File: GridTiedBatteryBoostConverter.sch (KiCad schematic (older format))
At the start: 58 parts, among them J101 Battery Connection, J103 Solar Panels, Q101 IXFP36N20X3, Q102 BC847B-13-F, Q103 SSM3K329R, Q104 SSM3J334R, U101 OPA2837DGK, U102 UCC2800DTR

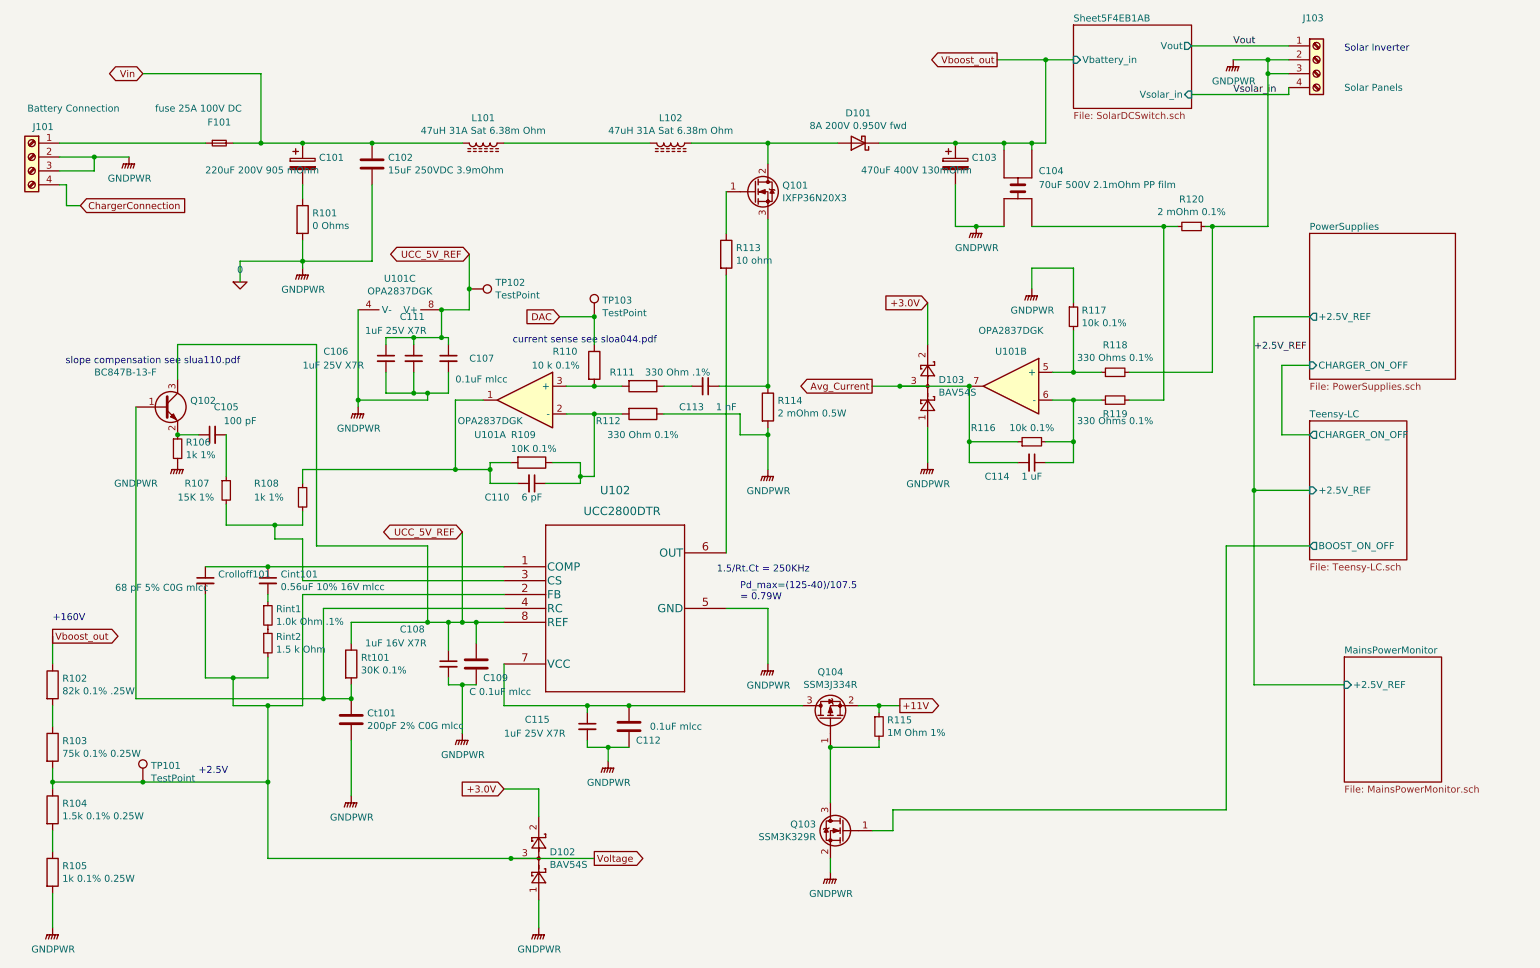
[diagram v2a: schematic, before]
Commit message: Consolidated a lot of part values that were the same part but not detected the same by Boms_away BOM editor because of subtle differences in how I specified the values. Added Digi-key part numbers to the resistors. Replaced 2mOhm .5W current sense resistors with 1W 2mOhm Thin Film resistors (lower inductance than metal element), And fixed a bug where I was earthing the return feed of the Solar inverter before passing through the current sense resistor.
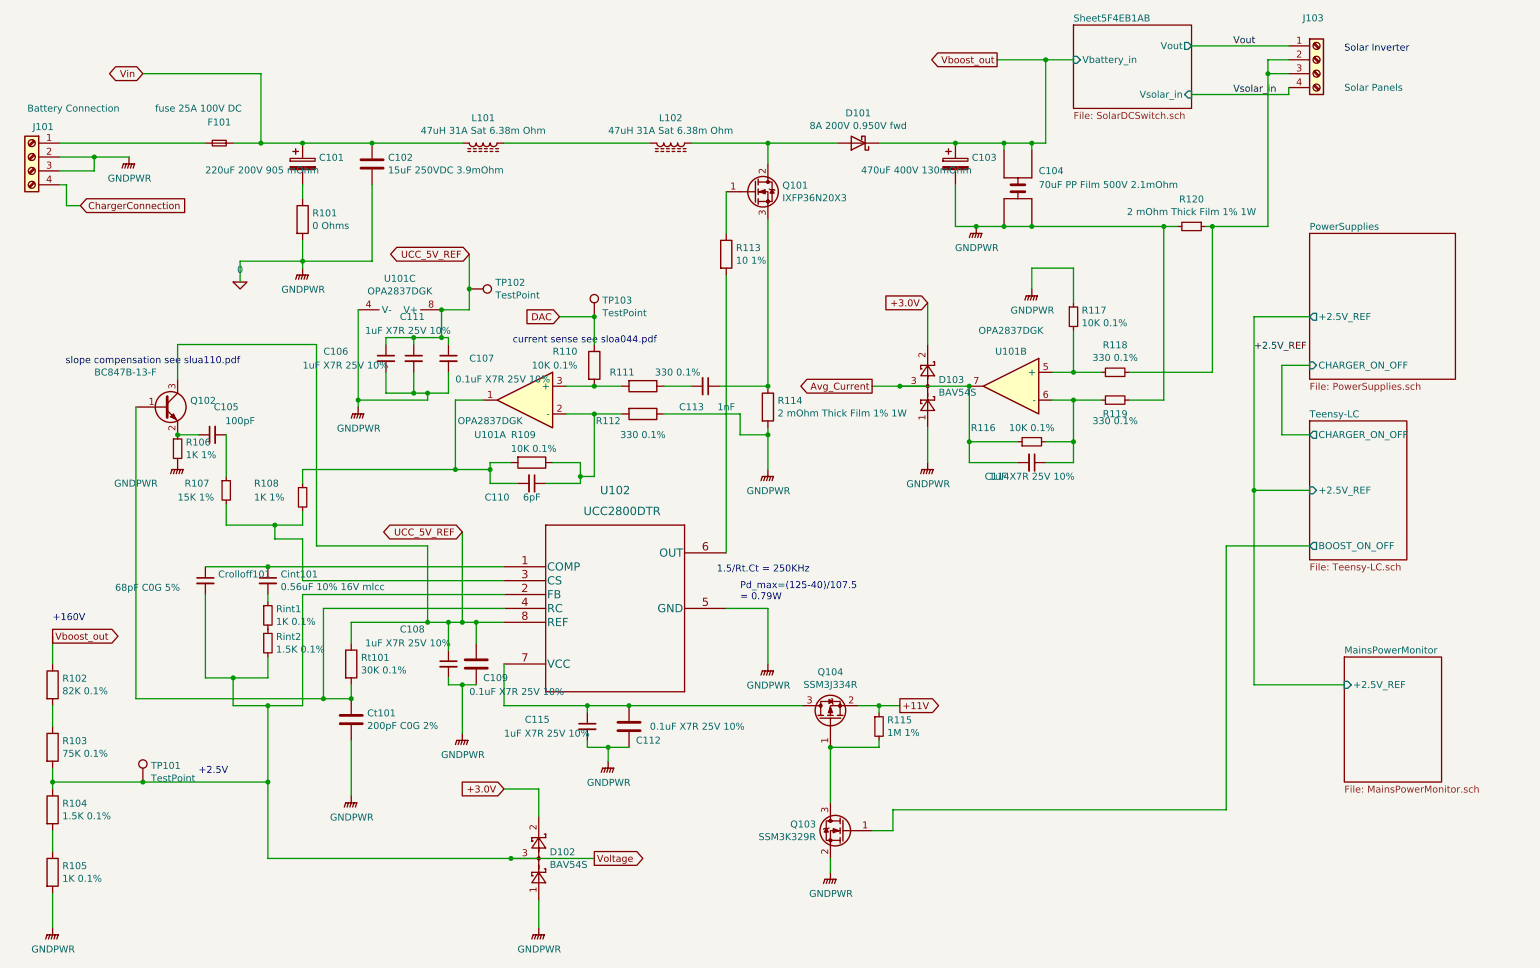
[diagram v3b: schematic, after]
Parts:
- C101, C102, C103, Cint101, D101, D102, D103, F101, J101, J103, L102, Q101, Q102, Q103, Q104, TP101, TP102, TP103, U101, U102: MFR (none) -> -; MPN (none) -> -; SPN (none) -> -; SPR (none) -> -; SPURL (none) -> -
- C104: value 70uF 500V 2.1mOhm PP film -> 70uF PP Film 500V 2.1mOhm; MFR (none) -> -; MPN (none) -> -; SPN (none) -> -; SPR (none) -> -; SPURL (none) -> -
- C105: value 100 pF -> 100pF; MFR (none) -> -; MPN (none) -> -; SPN (none) -> -; SPR (none) -> -; SPURL (none) -> -
- C106, C111, C115: value 1uF 25V X7R -> 1uF X7R 25V 10%; MFR (none) -> Wurth Elektronik; MPN (none) -> 885012207078; SPN (none) -> 732-7672-1-ND; SPR (none) -> digikey; SPURL (none) -> -
- C107, C112: value 0.1uF mlcc -> 0.1uF X7R 25V 10%; MFR (none) -> Samsung; MPN (none) -> CL21B104KACNNNC; SPN (none) -> 1276-1099-1-ND; SPR (none) -> digikey; SPURL (none) -> -
- C108: value 1uF 16V X7R -> 1uF X7R 25V 10%; MFR (none) -> Wurth Elektronik; MPN (none) -> 885012207078; SPN (none) -> 732-7672-1-ND; SPR (none) -> digikey; SPURL (none) -> -
- C109: value C 0.1uF mlcc -> 0.1uF X7R 25V 10%; MFR (none) -> Samsung; MPN (none) -> CL21B104KACNNNC; SPN (none) -> 1276-1099-1-ND; SPR (none) -> digikey; SPURL (none) -> -
- C110: value 6 pF -> 6pF; MFR (none) -> -; MPN (none) -> -; SPN (none) -> -; SPR (none) -> -; SPURL (none) -> -
- C113: value 1 nF -> 1nF; MFR (none) -> -; MPN (none) -> -; SPN (none) -> -; SPR (none) -> -; SPURL (none) -> -
- C114: value 1 uF -> 1uF X7R 25V 10%; MFR (none) -> Wurth Elektronik; MPN (none) -> 885012207078; SPN (none) -> 732-7672-1-ND; SPR (none) -> digikey; SPURL (none) -> -
- Crolloff101: value 68 pF 5% C0G mlcc -> 68pF C0G 5%; MFR (none) -> -; MPN (none) -> -; SPN (none) -> -; SPR (none) -> -; SPURL (none) -> -
- Ct101: value 200pF 2% C0G mlcc -> 200pF C0G 2%; MFR (none) -> AVX Corporation; MPN (none) -> 08051A201GAT2A; SPN (none) -> 478-10384-1-ND; SPR (none) -> digikey; SPURL (none) -> -
- L101: value 47uH 31A Sat 6.38m Ohm -> 47uH 31A Sat 6.38m Ohm; MFR (none) -> -; MPN (none) -> -; SPN (none) -> -; SPR (none) -> -; SPURL (none) -> -
- R101: MFR (none) -> Stackpole Electronics Inc; MPN (none) -> RMCF0805ZT0R00; SPN (none) -> RMCF0805ZT0R00CT-ND; SPR (none) -> digikey; SPURL (none) -> -
- R102: value 82k 0.1% .25W -> 82K 0.1%; MFR (none) -> Panasonic Electronic Components; MPN (none) -> ERA-6AEB823V; SPN (none) -> P82KDACT-ND; SPR (none) -> digikey; SPURL (none) -> -
- R103: value 75k 0.1% 0.25W -> 75K 0.1%; MFR (none) -> Panasonic Electronic Components; MPN (none) -> ERJ-PB6B7502V; SPN (none) -> P20808CT-ND; SPR (none) -> digikey; SPURL (none) -> -
- R104: value 1.5k 0.1% 0.25W -> 1.5K 0.1%; MFR (none) -> Panasonic Electronic Components; MPN (none) -> ERA-6AEB152V; SPN (none) -> P1.5KDACT-ND; SPR (none) -> digikey; SPURL (none) -> -
- R105: value 1k 0.1% 0.25W -> 1K 0.1%; MFR (none) -> Panasonic Electronic Components; MPN (none) -> ERA-6AEB102V; SPN (none) -> P1.0KDACT-ND; SPR (none) -> digikey; SPURL (none) -> -
- R106, R108: value 1k 1% -> 1K 1%; MFR (none) -> Yageo; MPN (none) -> RC0805FR-071KL; SPN (none) -> 311-1.00KCRCT-ND; SPR (none) -> digikey; SPURL (none) -> -
- R107: MFR (none) -> TE Connectivity Passive Product; MPN (none) -> CRGCQ0805F15K; SPN (none) -> A129763CT-ND; SPR (none) -> digikey; SPURL (none) -> -
- R109: MFR (none) -> Panasonic Electronic Components; MPN (none) -> ERA-6AEB103V; SPN (none) -> P10KDACT-ND; SPR (none) -> digikey; SPURL (none) -> -
- R110: value 10 k 0.1% -> 10K 0.1%; MFR (none) -> Panasonic Electronic Components; MPN (none) -> ERA-6AEB103V; SPN (none) -> P10KDACT-ND; SPR (none) -> digikey; SPURL (none) -> -
- R111: value 330 Ohm .1% -> 330 0.1%; MFR (none) -> Panasonic Electronic Components; MPN (none) -> ERA-6AEB331V; SPN (none) -> P330DACT-ND; SPR (none) -> digikey; SPURL (none) -> -
- R112: value 330 Ohm 0.1% -> 330 0.1%; MFR (none) -> Panasonic Electronic Components; MPN (none) -> ERA-6AEB331V; SPN (none) -> P330DACT-ND; SPR (none) -> digikey; SPURL (none) -> -
- R113: value 10 ohm -> 10 1%; MFR (none) -> Yageo; MPN (none) -> RC0805FR-0710RL; SPN (none) -> 311-10.0CRCT-ND; SPR (none) -> digikey; SPURL (none) -> -
- R114: value 2 mOhm 0.5W -> 2 mOhm Thick Film 1% 1W; footprint Resistors_SMD:R_0805_HandSoldering -> Resistors_SMD:R_1210_HandSoldering; MFR (none) -> Rohm Semiconductor; MPN (none) -> PMR25HZPFV2L00; SPN (none) -> RHM.002APCT-ND; SPR (none) -> digikey; SPURL (none) -> -
- R115: value 1M Ohm 1% -> 1M 1%; MFR (none) -> Yageo; MPN (none) -> RC0805FR-071ML; SPN (none) -> 311-1.00MCRCT-ND; SPR (none) -> digikey; SPURL (none) -> -
- R116, R117: value 10k 0.1% -> 10K 0.1%; MFR (none) -> Panasonic Electronic Components; MPN (none) -> ERA-6AEB103V; SPN (none) -> P10KDACT-ND; SPR (none) -> digikey; SPURL (none) -> -
- R118, R119: value 330 Ohms 0.1% -> 330 0.1%; MFR (none) -> Panasonic Electronic Components; MPN (none) -> ERA-6AEB331V; SPN (none) -> P330DACT-ND; SPR (none) -> digikey; SPURL (none) -> -
- R120: value 2 mOhm 0.1% -> 2 mOhm Thick Film 1% 1W; footprint Resistors_SMD:R_0805_HandSoldering -> Resistors_SMD:R_1210_HandSoldering; MFR (none) -> Rohm Semiconductor; MPN (none) -> PMR25HZPFV2L00; SPN (none) -> RHM.002APCT-ND; SPR (none) -> digikey; SPURL (none) -> -
- Rint1: value 1.0k Ohm .1% -> 1K 0.1%; MFR (none) -> Panasonic Electronic Components; MPN (none) -> ERA-6AEB102V; SPN (none) -> P1.0KDACT-ND; SPR (none) -> digikey; SPURL (none) -> -
- Rint2: value 1.5 k Ohm -> 1.5K 0.1%; MFR (none) -> Panasonic Electronic Components; MPN (none) -> ERA-6AEB152V; SPN (none) -> P1.5KDACT-ND; SPR (none) -> digikey; SPURL (none) -> -
- Rt101: MFR (none) -> Panasonic Electronic Components; MPN (none) -> ERA-6AEB303V; SPN (none) -> P30KDACT-ND; SPR (none) -> digikey; SPURL (none) -> -
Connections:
- net 0: now also C104.3, R119.2, R120.2; no longer J103.2 (Pin_2), J103.3 (Pin_3), R118.2, R120.1
- new net: J103.2 (Pin_2), J103.3 (Pin_3), R118.2, R120.1

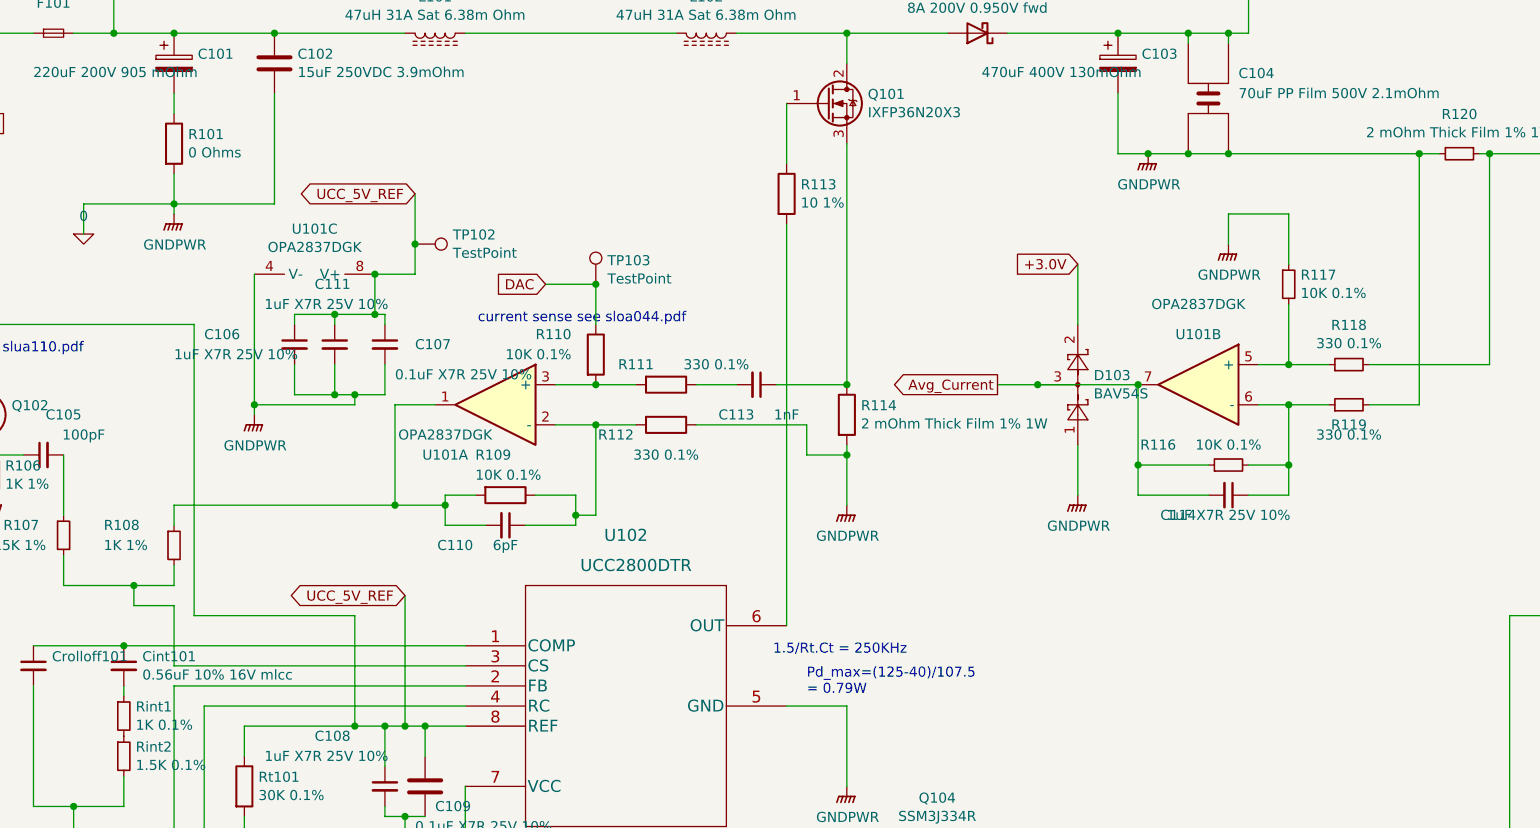
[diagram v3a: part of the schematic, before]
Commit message: change a few compoents foot prints for SOT23 to SOT23-Handsoldered, and SOT23-5 to SOT23-5-Handsoldered
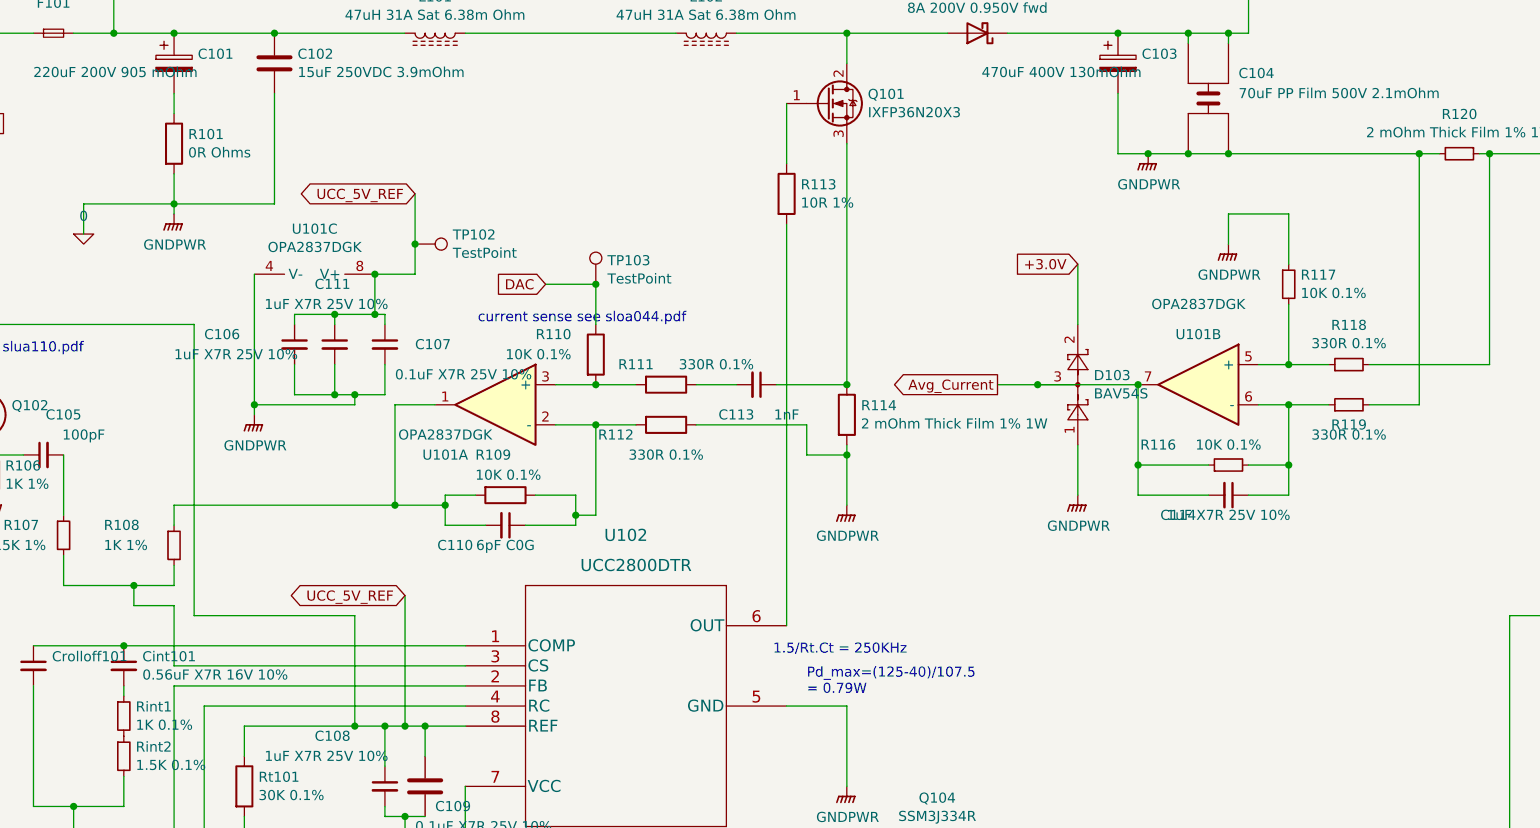
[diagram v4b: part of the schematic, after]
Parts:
- C105: MFR - -> KEMET; MPN - -> C0805C101JAGAC7800; SPN - -> 399-15000-1-ND; SPR - -> digikey
- C110: value 6pF -> 6pF C0G; MFR - -> Yageo; MPN - -> CC0805CRNPO9BN6R0; SPN - -> 311-4149-1-ND; SPR - -> digikey
- C113: MFR - -> Yageo; MPN - -> CC0805KRX7R9BB102; SPN - -> 311-1127-1-ND; SPR - -> digikey
- Cint101: value 0.56uF 10% 16V mlcc -> 0.56uF X7R 16V 10%; MFR - -> KEMET; MPN - -> C0805C564K4RACTU; SPN - -> 399-10074-1-ND; SPR - -> dikikey
- Crolloff101: MFR - -> Wurth Elektronik; MPN - -> 885012007081; SPN - -> 732-12227-1-ND; SPR - -> digikey
- D102, D103: footprint Package_TO_SOT_SMD:SOT-23 -> Package_TO_SOT_SMD:SOT-23_Handsoldering
- R101: value 0 Ohms -> 0R Ohms
- R111, R112, R118, R119: value 330 0.1% -> 330R 0.1%
- R113: value 10 1% -> 10R 1%
